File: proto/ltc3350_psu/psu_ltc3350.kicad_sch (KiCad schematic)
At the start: 21 parts, among them Q1 Q_NMOS_DGS, Q2 Q_PMOS_DGS, Q3 Q_NMOS_DGS, U1 LTC3350

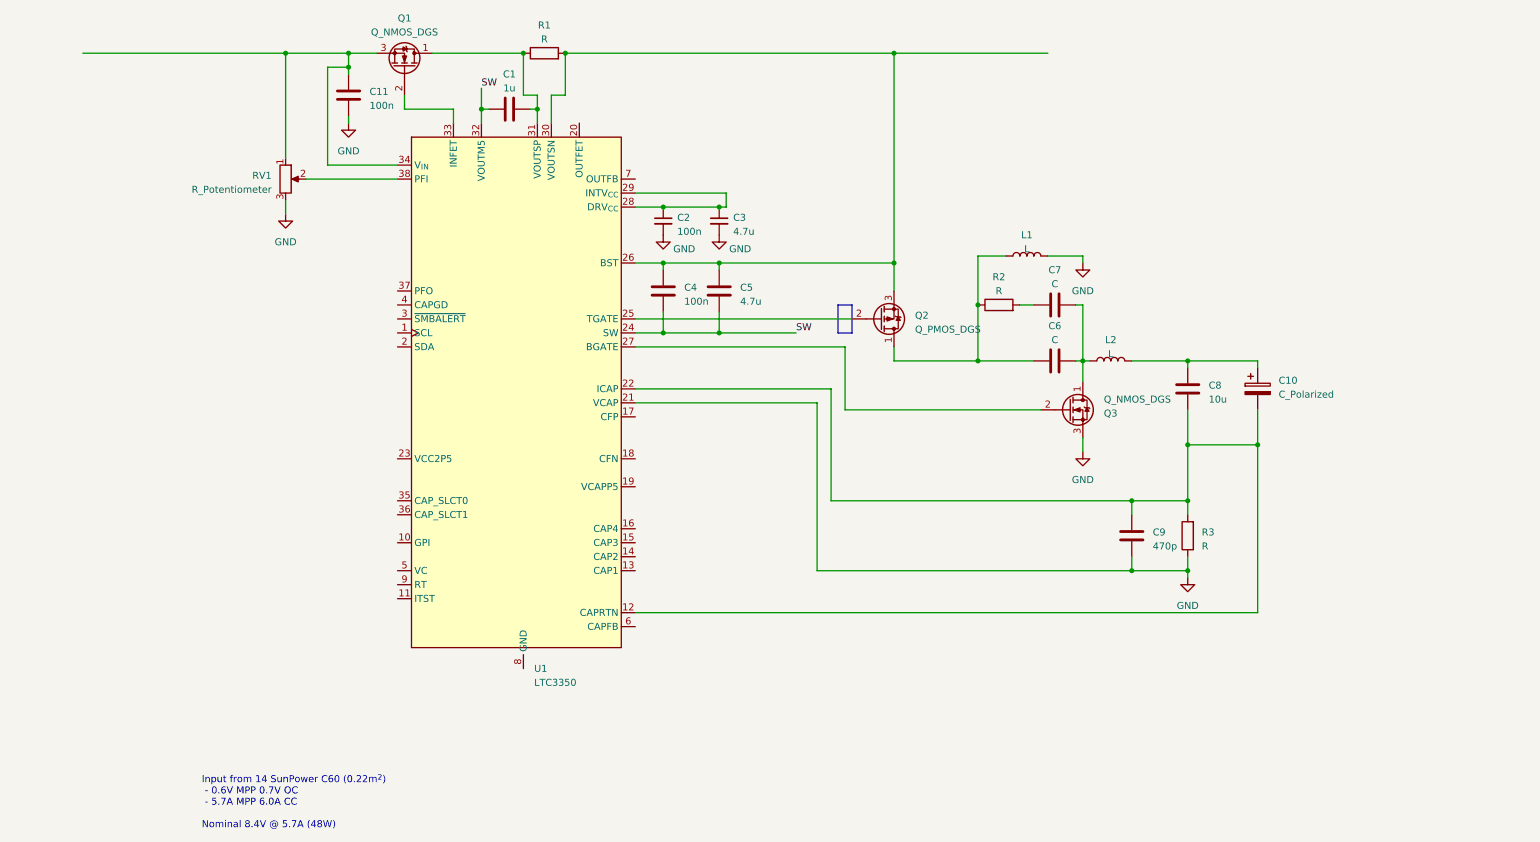
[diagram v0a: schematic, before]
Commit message: [ALIM] Update base alims
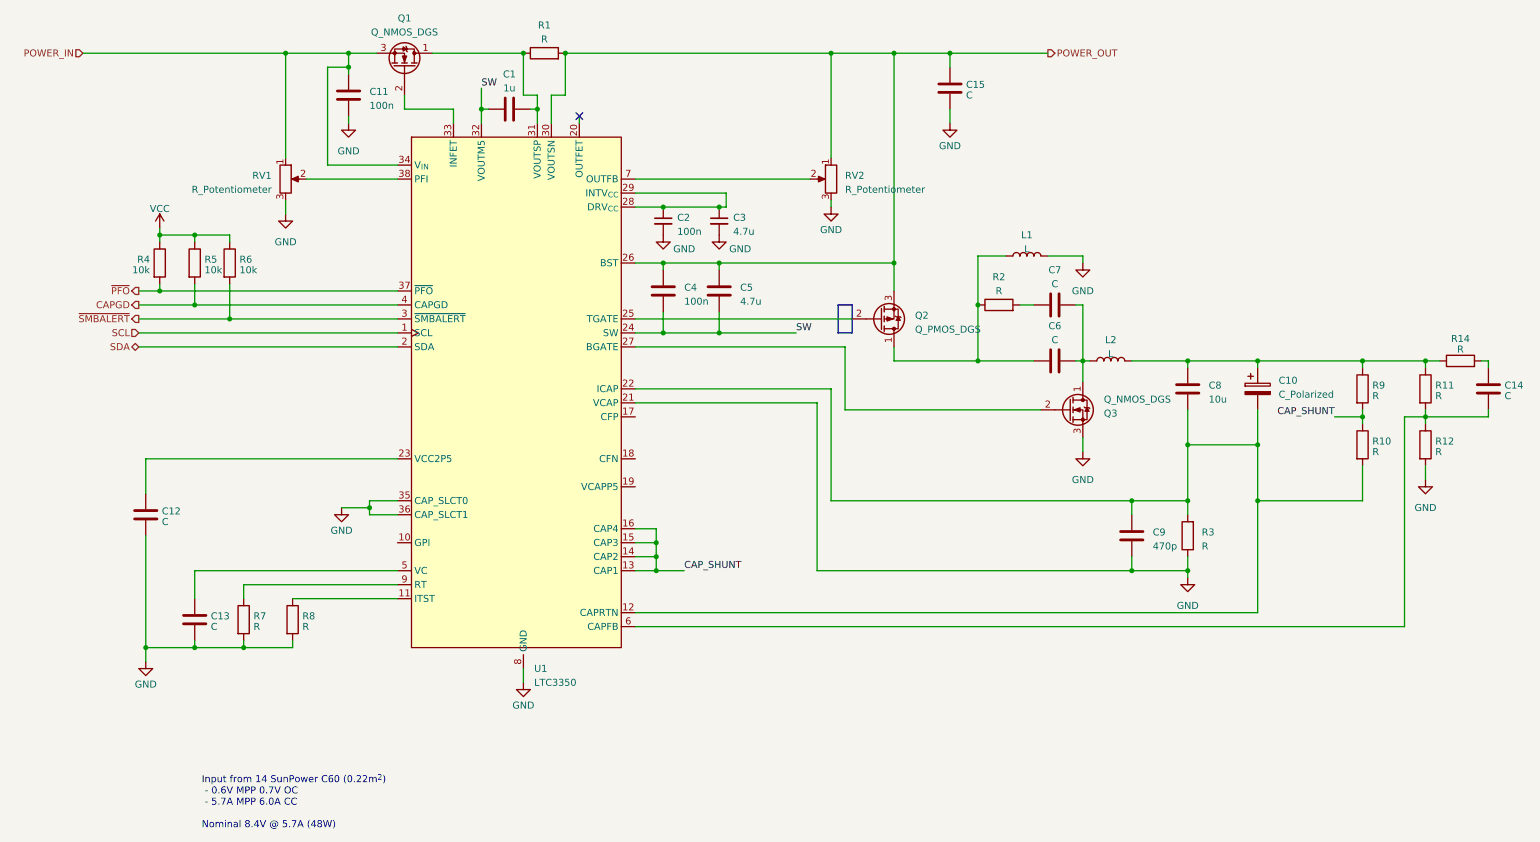
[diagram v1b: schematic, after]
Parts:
- added C12, C13, C14, C15: C, symbol Device:C
- added R10, R11, R12, R14, R7, R8, R9: R, symbol Device:R
- added R4, R5, R6: 10k, symbol Device:R
- added RV2: R_Potentiometer, symbol Device:R_Potentiometer
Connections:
- net GND: now also U1.35 (CAP_SLCT0), U1.36 (CAP_SLCT1), U1.39 (GND), U1.8 (GND), C12.2, C13.2, C15.2, R12.2, R7.2, R8.2, RV2.3
- net POWER_IN: now reaches C11.1, Q1.3 (S), RV1.1, U1.34 (V_{IN})
- net POWER_OUT: now reaches C4.1, C5.1, Q2.3 (S), R1.2, U1.26 (BST), U1.30 (VOUTSN)
- net POWER_OUT: now also C15.1, RV2.1
- net at C10.1, C8.1, L2.2: now also R11.1, R14.1, R9.1
- net at C10.2, C8.2, C9.1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: now also R10.2
- net SCL: now reaches U1.1 (SCL)
- net at U1.11 (ITST): now also R8.1
- net CAP_SHUNT: now reaches U1.13 (CAP1)
- net CAP_SHUNT: now also U1.14 (CAP2), U1.15 (CAP3), U1.16 (CAP4), R10.1, R9.2
- net SDA: now reaches U1.2 (SDA)
- net at U1.23 (VCC2P5): now also C12.1
- net ~{SMBALERT}: now reaches U1.3 (~{SMBALERT})
- net ~{SMBALERT}: now also R6.2
- net ~{PFO}: now reaches U1.37 (~{PFO})
- net ~{PFO}: now also R4.2
- net CAPGD: now reaches U1.4 (CAPGD)
- net CAPGD: now also R5.2
- net at U1.5 (VC): now also C13.1
- net at U1.6 (CAPFB): now also C14.2, R11.2, R12.1
- net at U1.7 (OUTFB): now also RV2.2
- net at U1.9 (RT): now also R7.1
- new net: C14.1, R14.2
- new net VCC: R4.1, R5.1, R6.1
- no-connect marks 0 -> 1
